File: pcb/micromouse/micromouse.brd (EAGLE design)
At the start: 80 x 115 mm, 70 parts, among them IC1 LM2575-5.0WU-(TR), IC2 LM2575-3.3WU-(TR), IC3 DSPIC33FJ64MC804-PT, IC4 L293D, Y1 7.3728MHz

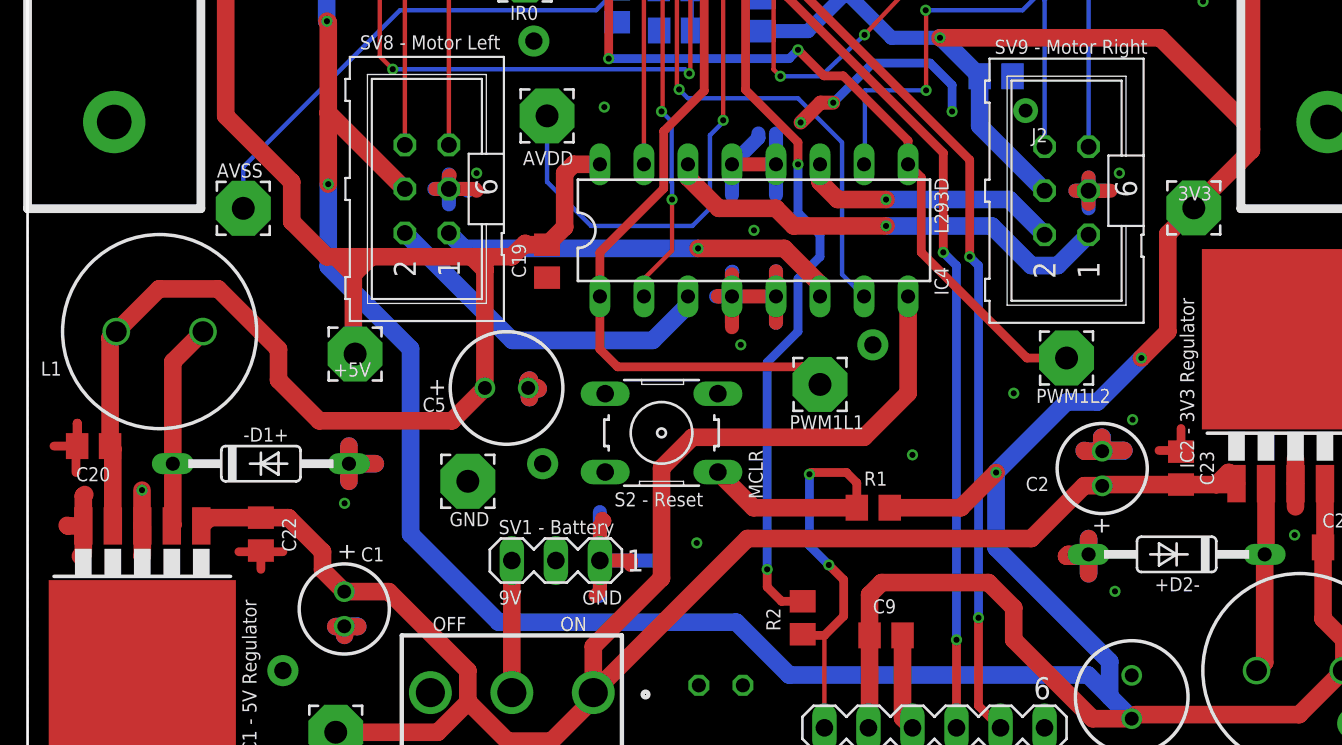
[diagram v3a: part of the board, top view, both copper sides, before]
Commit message: Improved connection out of 5V regulator in star connection + added one ground via
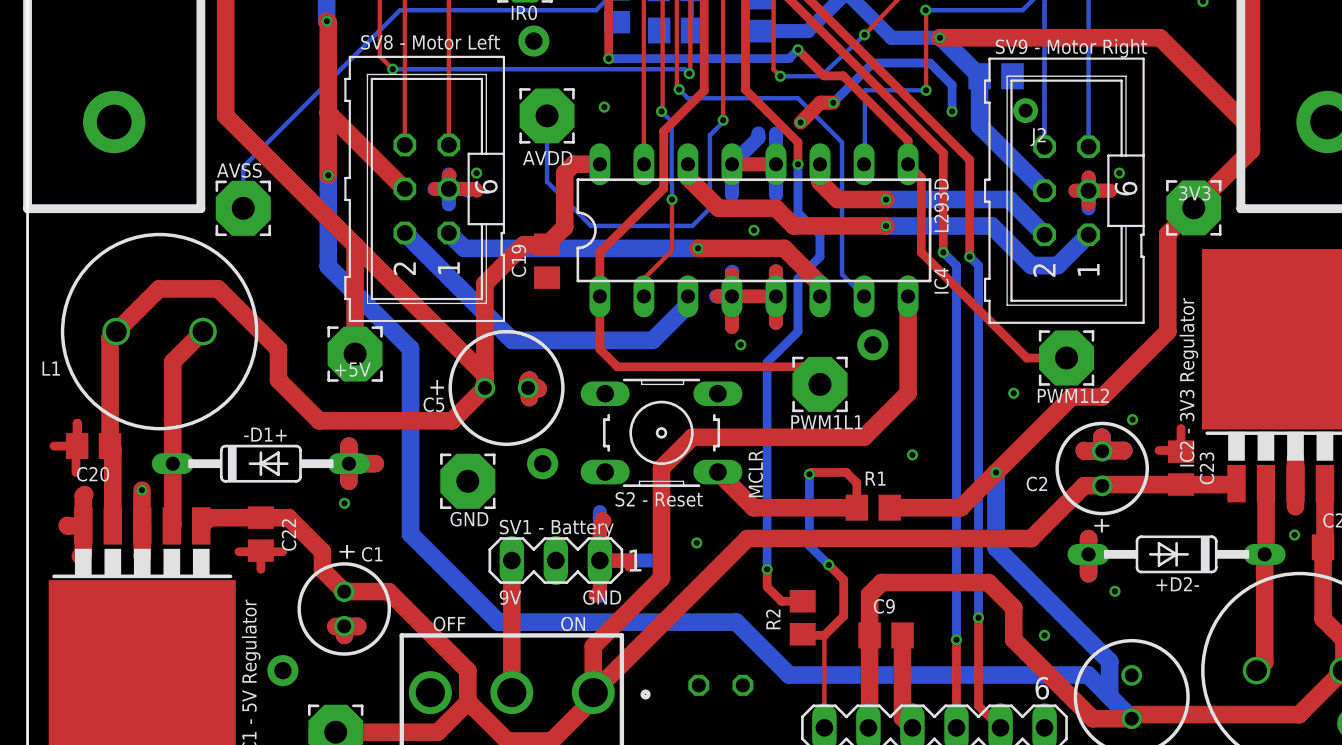
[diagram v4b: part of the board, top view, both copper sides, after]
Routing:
- net GND: track 171.5 -> 167.5 mm, vias 58 -> 59
- net +5V: track 208.9 -> 206.5 mm
- net +9V: track 118.9 -> 117.8 mm
- net +3V3: vias 10 -> 9
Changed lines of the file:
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@@
 <drawing>
 <settings>
-<setting alwaysvectorfont="yes"/>
+<setting alwaysvectorfont="no"/>
 <setting verticaltext="up"/>
 </settings>
@@
 <contactref element="C22" pad="1"/>
 <contactref element="C23" pad="1"/>
-<wire x1="61.214" y1="13.0556" x2="60.0456" y2="13.0556" width="1.016" layer="1"/>
-<wire x1="60.0456" y1="13.0556" x2="59.944" y2="12.954" width="1.016" layer="1"/>
-<wire x1="61.1124" y1="12.954" x2="59.944" y2="12.954" width="1.016" layer="1"/>
-<wire x1="61.1124" y1="12.954" x2="61.214" y2="13.0556" width="1.016" layer="1"/>
 <wire x1="61.214" y1="13.0556" x2="61.214" y2="11.938" width="1.016" layer="1"/>
 <wire x1="61.214" y1="11.938" x2="61.214" y2="13.0556" width="1.016" layer="16"/>
 <wire x1="61.214" y1="13.97" x2="61.214" y2="13.0556" width="1.016" layer="1"/>
 <wire x1="61.214" y1="13.0556" x2="61.214" y2="13.97" width="1.016" layer="16"/>
-<wire x1="61.214" y1="13.0556" x2="61.1124" y2="12.954" width="1.016" layer="16"/>
-<wire x1="61.1124" y1="12.954" x2="59.944" y2="12.954" width="1.016" layer="16"/>
 <wire x1="62.0014" y1="19.0086" x2="61.976" y2="19.034" width="1.016" layer="16"/>
 <wire x1="61.976" y1="19.034" x2="61.976" y2="19.812" width="1.016" layer="16"/>
@@
 <via x="67.818" y="44.958" extent="1-16" drill="0.35"/>
 <via x="59.944" y="87.376" extent="1-16" drill="0.35"/>
+<via x="58.674" y="8.382" extent="1-16" drill="0.35"/>
 </signal>
 <signal name="AVDD">
@@
 <contactref element="PAD4" pad="1"/>
 <wire x1="73.366" y1="3.81" x2="75.906" y2="6.35" width="1.016" layer="1"/>
-<via x="64.262" y="24.384" extent="1-16" drill="0.35"/>
 <wire x1="48.58" y1="8.382" x2="48.58" y2="3.114" width="1.016" layer="1"/>
 <wire x1="48.58" y1="3.114" x2="48.514" y2="3.048" width="1.016" layer="1"/>
@@
 <wire x1="63.9372" y1="3.81" x2="63.7032" y2="3.576" width="1.016" layer="1"/>
 <wire x1="73.366" y1="3.81" x2="63.9372" y2="3.81" width="1.016" layer="1"/>
-<wire x1="59.944" y1="21.844" x2="55.88" y2="17.78" width="1.016" layer="16"/>
-<wire x1="64.262" y1="24.384" x2="61.722" y2="21.844" width="1.016" layer="16"/>
-<wire x1="61.722" y1="21.844" x2="59.944" y2="21.844" width="1.016" layer="16"/>
 <wire x1="58.5176" y1="93.0616" x2="58.5176" y2="93.3156" width="1.016" layer="1"/>
 <wire x1="58.5176" y1="93.3156" x2="60.198" y2="94.996" width="1.016" layer="1"/>
@@
 <wire x1="54.93" y1="37.78" x2="54.93" y2="40.64" width="1.016" layer="16"/>
 <via x="52.644" y="42.86" extent="1-16" drill="0.35"/>
-<wire x1="64.262" y1="24.384" x2="65.786" y2="25.908" width="1.016" layer="1"/>
 <wire x1="65.786" y1="31.5468" x2="67.2846" y2="33.0454" width="1.016" layer="1"/>
 <wire x1="65.786" y1="25.908" x2="65.786" y2="31.5468" width="1.016" layer="1"/>
@@
 <wire x1="27.178" y1="9.144" x2="22.098" y2="14.224" width="1.016" layer="16"/>
 <wire x1="22.098" y1="24.9174" x2="22.098" y2="14.224" width="1.016" layer="16"/>
-<via x="17.3482" y="34.417" extent="1-16" drill="0.35"/>
-<wire x1="17.3482" y1="34.417" x2="17.3482" y2="29.6672" width="1.016" layer="16"/>
+<via x="17.3482" y="34.925" extent="1-16" drill="0.35"/>
+<wire x1="17.3482" y1="34.925" x2="17.3482" y2="29.6672" width="1.016" layer="16"/>
 <wire x1="17.3482" y1="29.6672" x2="22.098" y2="24.9174" width="1.016" layer="16"/>
 <wire x1="65.344" y1="42.86" x2="70.612" y2="37.592" width="1.016" layer="1"/>
@@
 <wire x1="17.2568" y1="46.6598" x2="17.2568" y2="43.8302" width="1.016" layer="16"/>
 <wire x1="17.2568" y1="43.8302" x2="17.272" y2="43.815" width="1.016" layer="16"/>
-<wire x1="17.3482" y1="38.5318" x2="17.3482" y2="34.417" width="1.016" layer="1"/>
+<wire x1="17.3482" y1="38.5318" x2="17.3482" y2="34.925" width="1.016" layer="1"/>
 <contactref element="C21" pad="2"/>
 <wire x1="55.438" y1="11.43" x2="49.276" y2="11.43" width="1.016" layer="1"/>
@@
 <wire x1="75.946" y1="8.128" x2="75.946" y2="6.39" width="1.016" layer="1"/>
 <wire x1="75.946" y1="6.39" x2="75.906" y2="6.35" width="1.016" layer="1"/>
+<wire x1="55.88" y1="17.78" x2="60.2385" y2="22.1385" width="1.016" layer="1"/>
+<wire x1="60.2385" y1="22.1385" x2="62.0165" y2="22.1385" width="1.016" layer="1"/>
+<wire x1="62.0165" y1="22.1385" x2="65.786" y2="25.908" width="1.016" layer="1"/>
 </signal>
 <signal name="AVSS">
@@
 <contactref element="L1" pad="2"/>
 <contactref element="PAD3" pad="1"/>
-<wire x1="5.12" y1="25.908" x2="4.9182" y2="25.7062" width="1.016" layer="1"/>
 <wire x1="5.12" y1="25.908" x2="7.5838" y2="28.3718" width="1.016" layer="1"/>
 <wire x1="30.988" y1="35.052" x2="30.988" y2="31.938" width="1.016" layer="1"/>
@@
 <wire x1="33.02" y1="35.56" x2="31.496" y2="35.56" width="1.016" layer="1"/>
 <wire x1="31.496" y1="35.56" x2="30.988" y2="35.052" width="1.016" layer="1"/>
-<wire x1="29.972" y1="30.922" x2="28.72018125" y2="30.922" width="1.016" layer="1"/>
-<wire x1="28.72018125" y1="30.922" x2="28.709990625" y2="30.995990625" width="1.016" layer="1"/>
-<wire x1="28.709990625" y1="30.995990625" x2="27.94" y2="30.226" width="1.016" layer="1"/>
-<wire x1="27.94" y1="30.226" x2="26.67" y2="30.226" width="1.016" layer="1"/>
-<wire x1="26.67" y1="30.226" x2="25.654" y2="30.226" width="1.016" layer="1"/>
-<wire x1="25.654" y1="30.226" x2="19.812" y2="30.226" width="1.016" layer="1"/>
-<wire x1="19.812" y1="30.226" x2="18.796" y2="30.226" width="1.016" layer="1"/>
-<wire x1="18.796" y1="30.226" x2="18.034" y2="30.226" width="1.016" layer="1"/>
-<wire x1="18.034" y1="30.226" x2="17.272" y2="30.226" width="1.016" layer="1"/>
 <wire x1="41.91" y1="90.17" x2="53.594" y2="90.17" width="1.016" layer="1"/>
 <wire x1="53.594" y1="90.17" x2="55.372" y2="88.392" width="1.016" layer="1"/>
@@
 <wire x1="59.436" y1="79.756" x2="58.42" y2="78.74" width="1.016" layer="1"/>
 <contactref element="C5" pad="1"/>
-<wire x1="18.796" y1="29.21" x2="18.796" y2="24.7142" width="1.016" layer="1"/>
-<wire x1="18.8976" y1="24.6126" x2="18.796" y2="24.7142" width="1.016" layer="1"/>
-<wire x1="18.796" y1="30.226" x2="18.796" y2="29.21" width="1.016" layer="1"/>
-<wire x1="26.3852" y1="22.6568" x2="26.3852" y2="29.464" width="1.016" layer="1"/>
-<wire x1="26.3852" y1="29.464" x2="26.3852" y2="29.9412" width="1.016" layer="1"/>
-<wire x1="26.3852" y1="29.9412" x2="26.67" y2="30.226" width="1.016" layer="1"/>
-<wire x1="18.796" y1="29.21" x2="19.812" y2="30.226" width="1.016" layer="1"/>
-<wire x1="18.796" y1="29.21" x2="18.034" y2="29.972" width="1.016" layer="1"/>
-<wire x1="18.034" y1="29.972" x2="18.034" y2="30.226" width="1.016" layer="1"/>
-<wire x1="15.24" y1="32.258" x2="17.272" y2="30.226" width="1.016" layer="1"/>
-<wire x1="26.3852" y1="29.464" x2="25.654" y2="30.1952" width="1.016" layer="1"/>
-<wire x1="25.654" y1="30.1952" x2="25.654" y2="30.226" width="1.016" layer="1"/>
-<wire x1="11.43" y1="38.354" x2="15.24" y2="34.544" width="1.016" layer="1"/>
-<wire x1="15.24" y1="34.544" x2="15.24" y2="32.258" width="1.016" layer="1"/>
 <wire x1="11.43" y1="70.866" x2="11.43" y2="38.354" width="1.016" layer="1"/>
 <wire x1="22.606" y1="81.788" x2="25.4" y2="81.788" width="1.016" layer="1"/>
@@
 <wire x1="4.76" y1="19.304" x2="4.76" y2="25.548" width="1.016" layer="1"/>
 <wire x1="4.76" y1="25.548" x2="5.12" y2="25.908" width="1.016" layer="1"/>
+<wire x1="26.3852" y1="22.6568" x2="26.3852" y2="28.6712" width="1.016" layer="1"/>
+<wire x1="28.636" y1="30.922" x2="29.972" y2="30.922" width="1.016" layer="1"/>
+<wire x1="26.3852" y1="28.6712" x2="28.636" y2="30.922" width="1.016" layer="1"/>
+<wire x1="26.3852" y1="23.3988" x2="26.3852" y2="22.6568" width="1.016" layer="1"/>
+<wire x1="11.43" y1="38.354" x2="18.288" y2="31.496" width="1.016" layer="1"/>
+<wire x1="18.8976" y1="30.8864" x2="26.3852" y2="23.3988" width="1.016" layer="1"/>
+<wire x1="18.8976" y1="24.6126" x2="18.8976" y2="30.8864" width="1.016" layer="1"/>
+<wire x1="18.8976" y1="30.8864" x2="18.288" y2="31.496" width="1.016" layer="1"/>
 </signal>
 <signal name="IR2">
@@
 <wire x1="69.6968" y1="17.084" x2="68.58" y2="17.084" width="1.016" layer="1"/>
 <wire x1="68.58" y1="17.084" x2="66.548" y2="17.084" width="1.016" layer="1"/>
-<wire x1="68.58" y1="17.084" x2="69.276" y2="17.78" width="1.016" layer="1"/>
-<wire x1="69.276" y1="17.78" x2="69.342" y2="17.78" width="1.016" layer="1"/>
 </signal>
 <signal name="N$4">

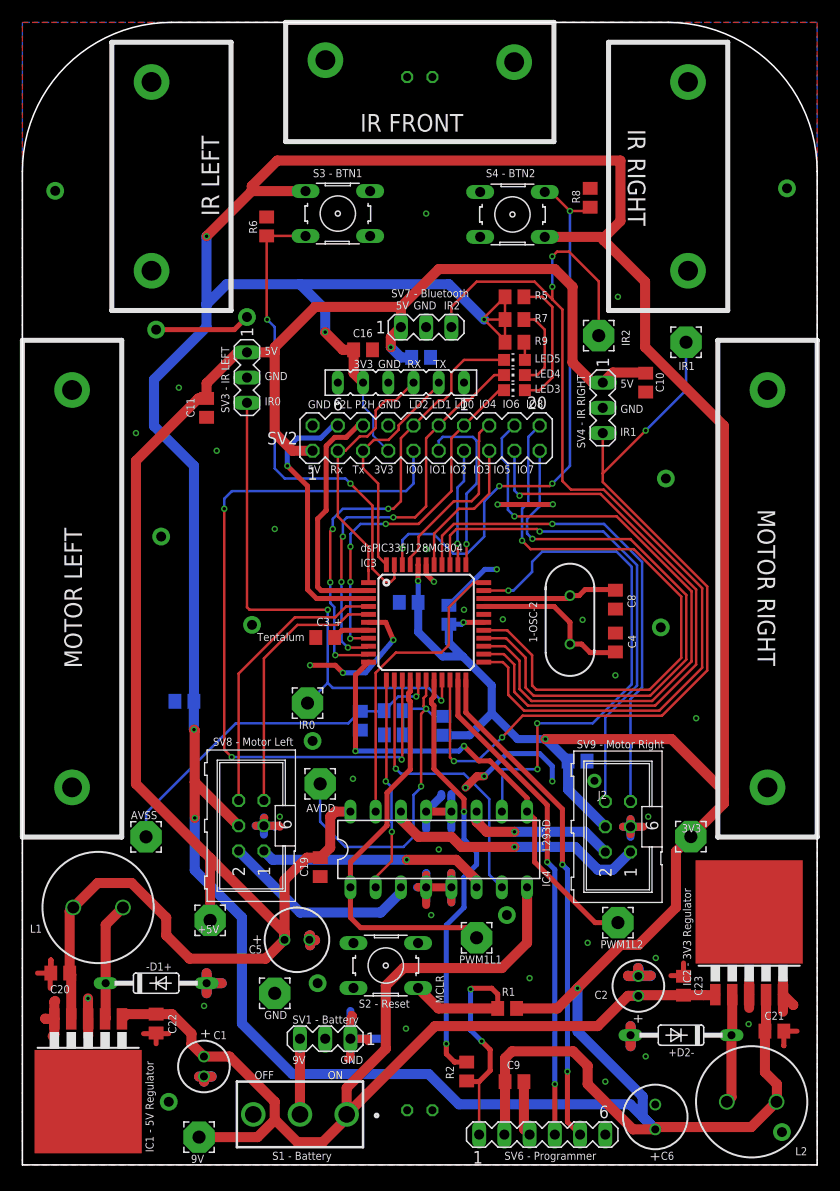
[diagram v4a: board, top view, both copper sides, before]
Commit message: Added low pass filter for distance sensors
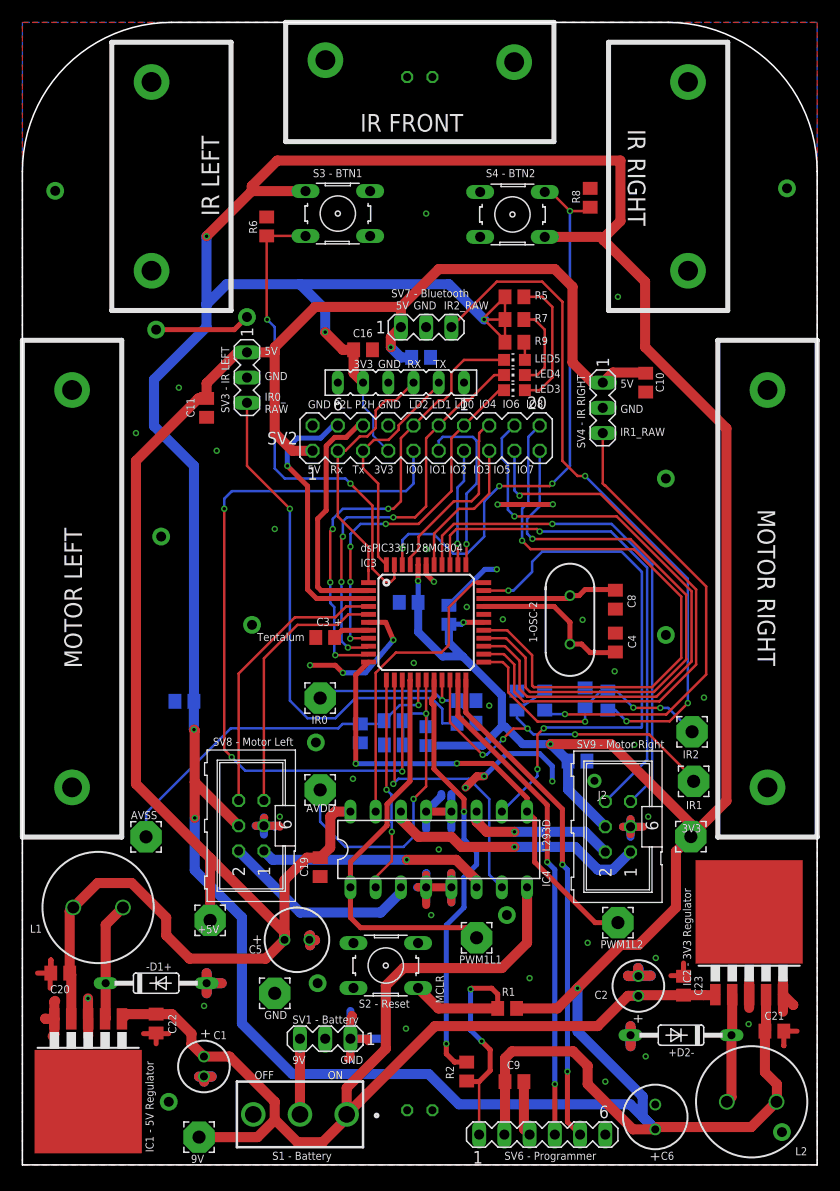
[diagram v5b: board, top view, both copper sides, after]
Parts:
- added C24, C25, C26: 10uF, rcl:C0805
- added R10, R11, R12: 16R, rcl:R0805
- moved PAD8 44.2 mm to (67.6, 38.6)
- moved PAD9 41.0 mm to (67.4, 43.6)
- moved R3 2.00 mm to (40.7, 43.2)
- moved PAD7 1.37 mm to (30.0, 47.0)
- moved R4 1.27 mm to (34.0, 43.4)
- moved C13 1.02 mm to (37.4, 44.7)
- moved C7 1.02 mm to (37.4, 42.3)
- moved PAD10 0.61 mm to (30.0, 37.7)
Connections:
- new net IR0_RAW: R10.2, SV3.3
- new net IR1_RAW: R11.2, SV4.3
- new net IR2_RAW: R12.2, SV5.3
- net GND: now also C24.1, C25.1, C26.1
- net IR0: now also C24.2, R10.1; no longer SV3.3
- net IR1: now also C25.2, R11.1; no longer SV4.3
- net IR2: now also C26.2, R12.1; no longer SV5.3
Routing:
- net IR2: track 102.5 -> 28.8 mm, vias 2 -> 3
- net IR2_RAW: track 0.00 -> 69.3 mm, vias 0 -> 3
- net IR0_RAW: track 0.00 -> 52.1 mm, vias 0 -> 1
- net IR1_RAW: track 0.00 -> 46.7 mm, vias 0 -> 1
- net IR1: track 82.5 -> 39.3 mm, vias 3 -> 4
- net IR0: track 53.3 -> 19.5 mm, vias 2 -> 1
- net IO0: track 74.6 -> 76.3 mm
- net +3V3: track 501.4 -> 503.0 mm
- net M1-_EN: track 29.1 -> 30.6 mm
- net M2+_EN: track 53.2 -> 54.7 mm
- net AVDD: track 38.2 -> 36.8 mm
- net ENC2_A: track 48.7 -> 50.0 mm
- net ENC2_B: track 49.7 -> 51.0 mm
- net AVSS: track 36.2 -> 36.9 mm
- net GND: vias 59 -> 62
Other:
- board text added: "C24"
- board text added: "C25"
- board text added: "C26"
- board text added: "IR0_ RAW"
- board text added: "IR1_RAW"
- board text added: "IR2_RAW"
- board text added: "R10"
- board text added: "R11"
- board text added: "R12"

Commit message: Remove extra GND connections or make them smaller. Remove typos. Make enough space for bluetooth module (9mm).
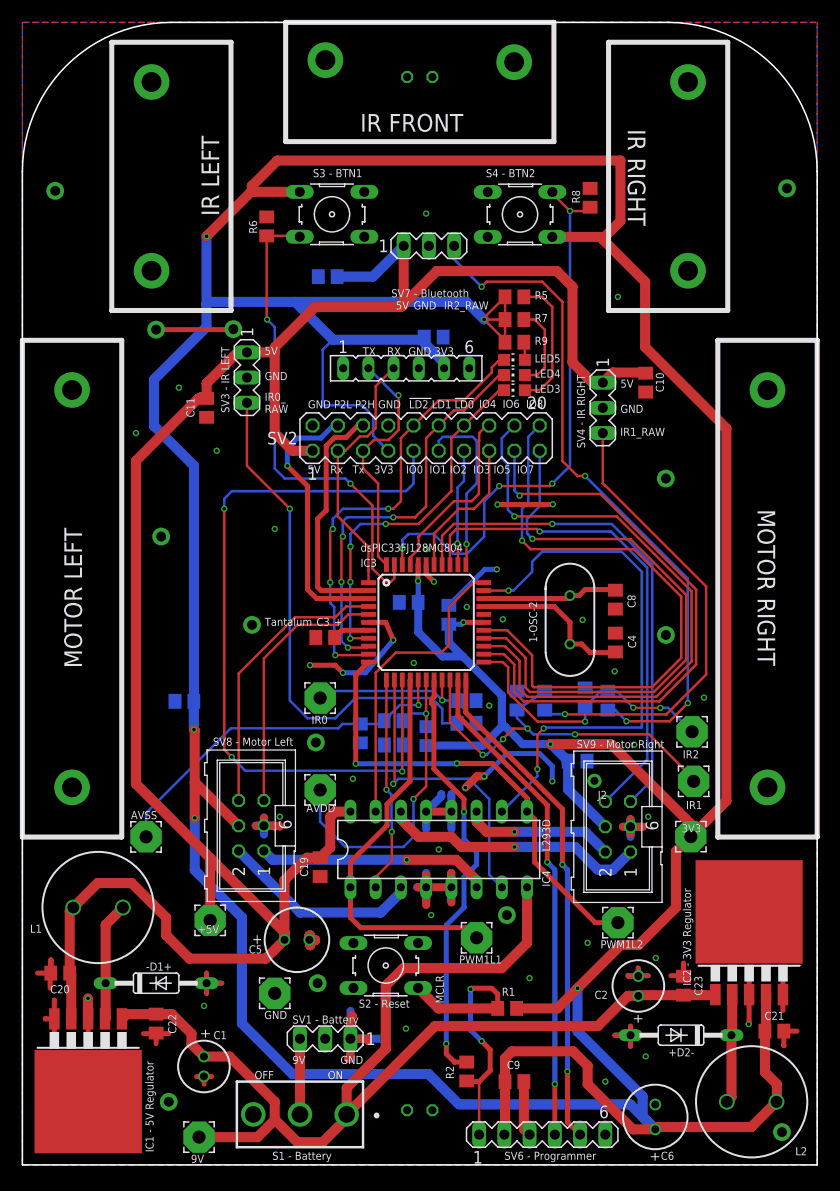
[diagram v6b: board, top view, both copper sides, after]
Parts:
- moved C12 12.4 mm to (30.7, 89.4), turned to 180 degrees
- moved SV5 8.18 mm to (40.9, 92.5)
- moved C16 7.22 mm to (41.4, 83.3), flipped to the bottom, turned to 0 degrees
- moved SV7 1.54 mm to (38.6, 80.2), turned to 0 degrees
- moved S4 0.76 mm to (50.1, 95.7)
- moved S3 0.59 mm to (31.2, 95.7)
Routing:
- net +3V3: track 503.0 -> 514.5 mm, vias 9 -> 8
- net +5V: track 206.5 -> 213.2 mm, vias 1 -> 0
- net TX: track 23.3 -> 24.5 mm, vias 0 -> 1
- net N_LED2: track 46.2 -> 45.3 mm
- net BTN_2: track 57.3 -> 56.7 mm
- net GND: track 167.5 -> 168.1 mm
- net BTN_1: track 49.7 -> 49.1 mm
- net IR2_RAW: track 69.3 -> 69.8 mm, vias 3 -> 4
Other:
- board text added: "Tantalum"
- board text removed: "Tentalum"
